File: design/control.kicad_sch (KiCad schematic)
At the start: 20 parts, among them J3 Conn-OScope, J3 SMB, J4 Conn-OScope, J4 SMA, J5 USB_C_Receptacle_USB2.0_14P, U1 STM32F303RETx, U4 CP2102N-Axx-xQFN20

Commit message: _
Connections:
- net HVSense renamed HVVS
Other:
- note added: "Will trip when HV_CS exceeds DAC1_OUT1"
- note removed: "Will trip when HV_CS exceeds 1.2V"
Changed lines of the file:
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@@
 		)
 	)
-	(text "Will trip when HV_CS\nexceeds 1.2V"
+	(text "Will trip when HV_CS\nexceeds DAC1_OUT1"
 		(exclude_from_sim no)
 		(at 248.92 128.27 0)
@@
 		)
 	)
-	(global_label "HVSense"
+	(global_label "HVVS"
 		(shape input)
 		(at 224.79 49.53 0)
@@
 		)
 		(property "Intersheetrefs" "${INTERSHEET_REFS}"
-			(at 235.7581 49.53 0)
+			(at 232.4924 49.53 0)
 			(effects
 				(font

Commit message: _
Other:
- note removed: "For a prototype it might be worth breaking out a few extra GPIO pins..."
- note removed: "I could also set a custom threshold for this with the DAC whichcwould probably improve resolution"
- note removed: "It might make more sense for PulseSense to go to a comparator, since it could also stop the HV generation when the switch is closed"
- note removed: "Same board that came with the devkit I ordered"
- moved on the sheet: J5, R4, R6, R7, U4

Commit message: Working on high voltage switching
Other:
- company: UNH Resilient Architecture Lab -> University of New Hampshire, Resilient Architecture Lab
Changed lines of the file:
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@@
 		(title "BitCrusher: Affordable, Open Source EMFI Platform")
 		(rev "0.1")
-		(company "UNH Resilient Architecture Lab")
+		(company "University of New Hampshire, Resilient Architecture Lab")
 		(comment 1 "Advisor: Dean Sullivan")
 		(comment 2 "Author: George Crane")

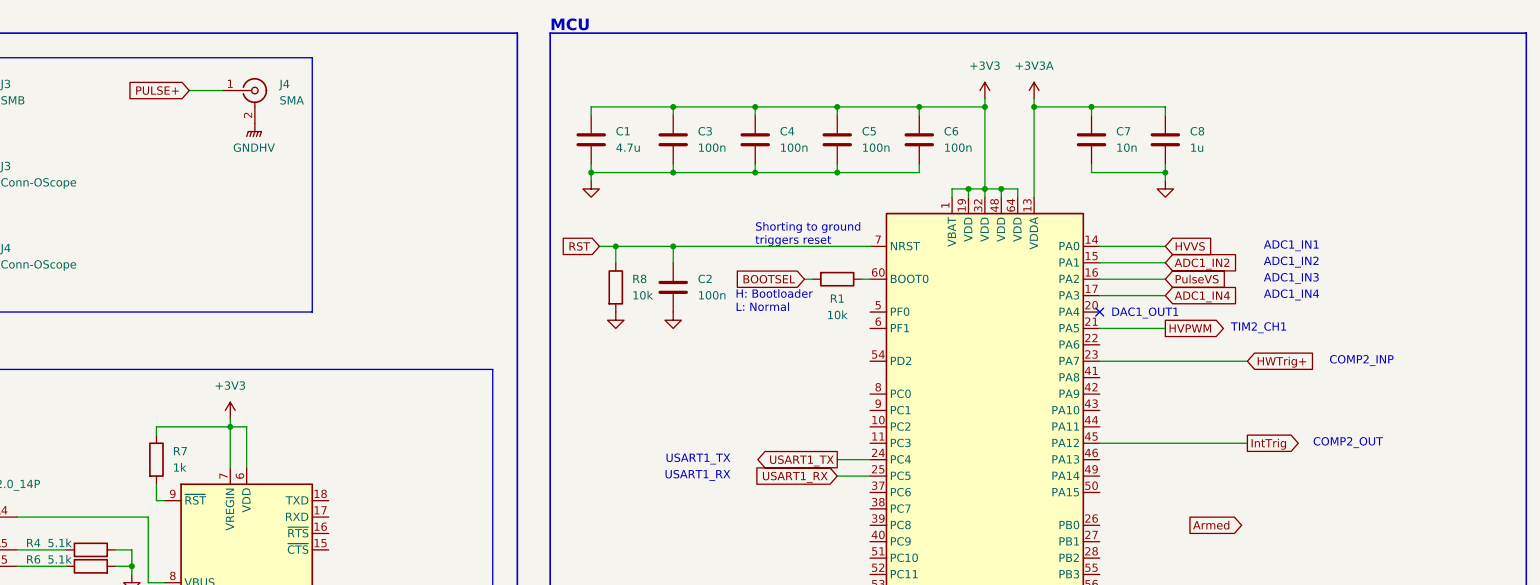
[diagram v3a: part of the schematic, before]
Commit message: assembling final components for HV switching
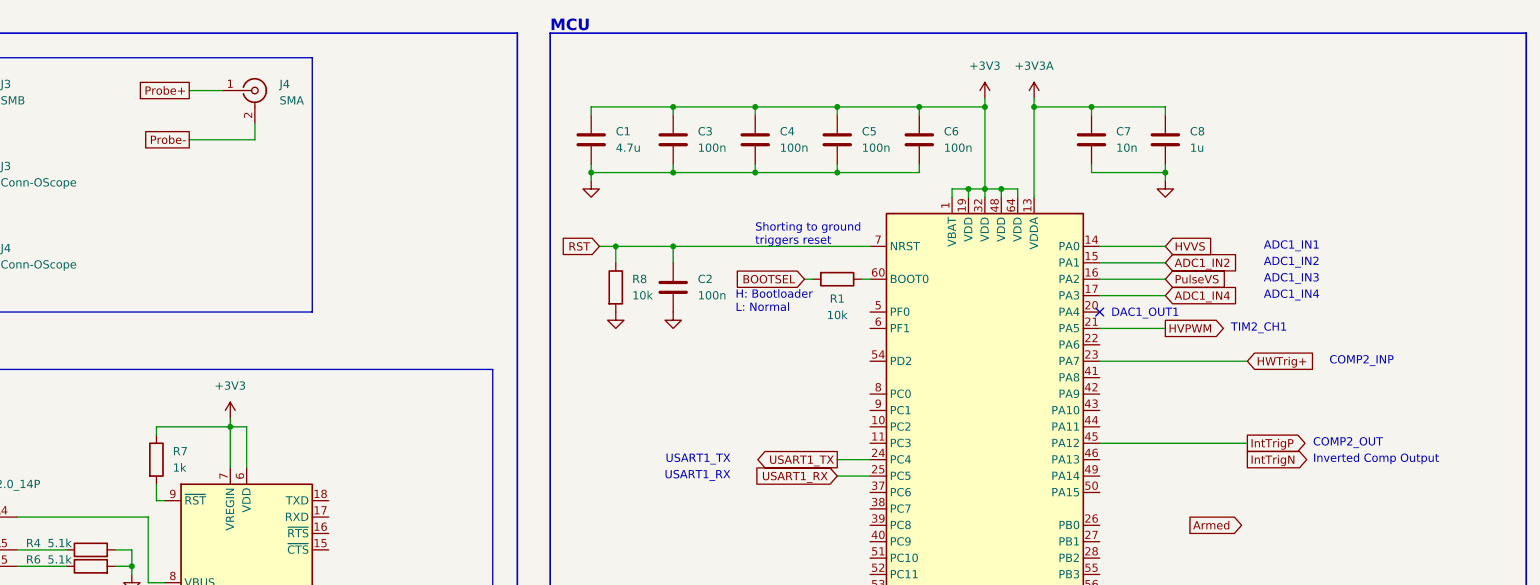
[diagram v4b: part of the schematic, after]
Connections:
- net GNDHV renamed Probe-
- net IntTrig renamed IntTrigP
- net PULSE+ renamed Probe+
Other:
- note added: "Inverted Comp Output"
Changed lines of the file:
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@@
+		)
+	)
+	(text "Inverted Comp Output"
+		(exclude_from_sim no)
+		(at 247.65 82.55 0)
+		(effects
+			(font
+				(size 1.27 1.27)
+			)
+			(justify left)
 		)
 	)
@@
 	(wire
 		(pts
+			(xy 83.82 33.02) (xy 83.82 30.48)
+		)
+		(stroke
+			(width 0)
+			(type default)
+		)
+	)
+	(wire
+		(pts
 			(xy 139.7 49.53) (xy 148.59 49.53)
 		)
@@
 		(pts
 			(xy 30.48 38.1) (xy 35.56 38.1)
+		)
+		(stroke
+			(width 0)
+			(type default)
+		)
+	)
+	(wire
+		(pts
+			(xy 73.66 33.02) (xy 83.82 33.02)
 		)
 		(stroke
@@
 		)
 	)
-	(global_label "IntTrig"
+	(global_label "IntTrigN"
+		(shape output)
+		(at 237.49 82.55 0)
+		(fields_autoplaced yes)
+		(effects
+			(font
+				(size 1.27 1.27)
+			)
+			(justify left)
+		)
+		(property "Intersheetrefs" "${INTERSHEET_REFS}"
+			(at 247.7928 82.55 0)
+			(effects
+				(font
+					(size 1.27 1.27)
+				)
+				(justify left)
+				(hide yes)
+			)
+		)
+	)
+	(global_label "Probe-"
+		(shape passive)
+		(at 73.66 33.02 180)
+		(fields_autoplaced yes)
+		(effects
+			(font
+				(size 1.27 1.27)
+			)
+			(justify right)
+		)
+		(property "Intersheetrefs" "${INTERSHEET_REFS}"
+			(at 64.7709 33.02 0)
+			(effects
+				(font
+					(size 1.27 1.27)
+				)
+				(justify right)
+				(hide yes)
+			)
+		)
+	)
+	(global_label "IntTrigP"
 		(shape output)
 		(at 237.49 80.01 0)
@@
 		)
 		(property "Intersheetrefs" "${INTERSHEET_REFS}"
-			(at 246.4623 80.01 0)
+			(at 247.7323 80.01 0)
 			(effects
 				(font
@@
 		)
 	)
-	(global_label "PULSE+"
-		(shape input)
+	(global_label "Probe+"
+		(shape passive)
 		(at 73.66 25.4 180)
 		(fields_autoplaced yes)
@@
 		)
 		(property "Intersheetrefs" "${INTERSHEET_REFS}"
-			(at 63.1153 25.4 0)
+			(at 64.7709 25.4 0)
 			(effects
 				(font
@@
 					(unit 1)
 				)
-			)
-		)
-	)
-	(symbol
-		(lib_id "power:GNDPWR")
-		(at 83.82 30.48 0)
-		(unit 1)
-		(exclude_from_sim no)
-		(in_bom yes)
-		(on_board yes)
-		(dnp no)
-		(fields_autoplaced yes)
-		(property "Reference" "#PWR018"
-			(at 83.82 35.56 0)
-			(effects
-				(font
-					(size 1.27 1.27)
-				)
-				(hide yes)
-			)
-		)
-		(property "Value" "GNDHV"
-			(at 83.693 34.29 0)
-			(effects
-				(font
-					(size 1.27 1.27)
-				)
-			)
-		)
-		(property "Footprint" ""
-			(at 83.82 31.75 0)
-			(effects
-				(font
-					(size 1.27 1.27)
-				)
-				(hide yes)
-			)
-		)
-		(property "Datasheet" ""
-			(at 83.82 31.75 0)
-			(effects
-				(font
-					(size 1.27 1.27)
-				)
-				(hide yes)
-			)
-		)
-		(property "Description" "Power symbol creates a global label with name \"GNDPWR\" , global ground"
-			(at 83.82 30.48 0)
-			(effects
-				(font
-					(size 1.27 1.27)
-				)
-				(hide yes)
-			)
-		)
-		(pin "1"
-		)
-		(instances
-			(project "BitCrusher"
-				(path "/e1be550d-9ce6-42b1-a89a-c00b9d7586dd/29f45a98-1f25-4a6e-8231-3aa3a650ea17"
-					(reference "#PWR018")
-					(unit 1)
-				)

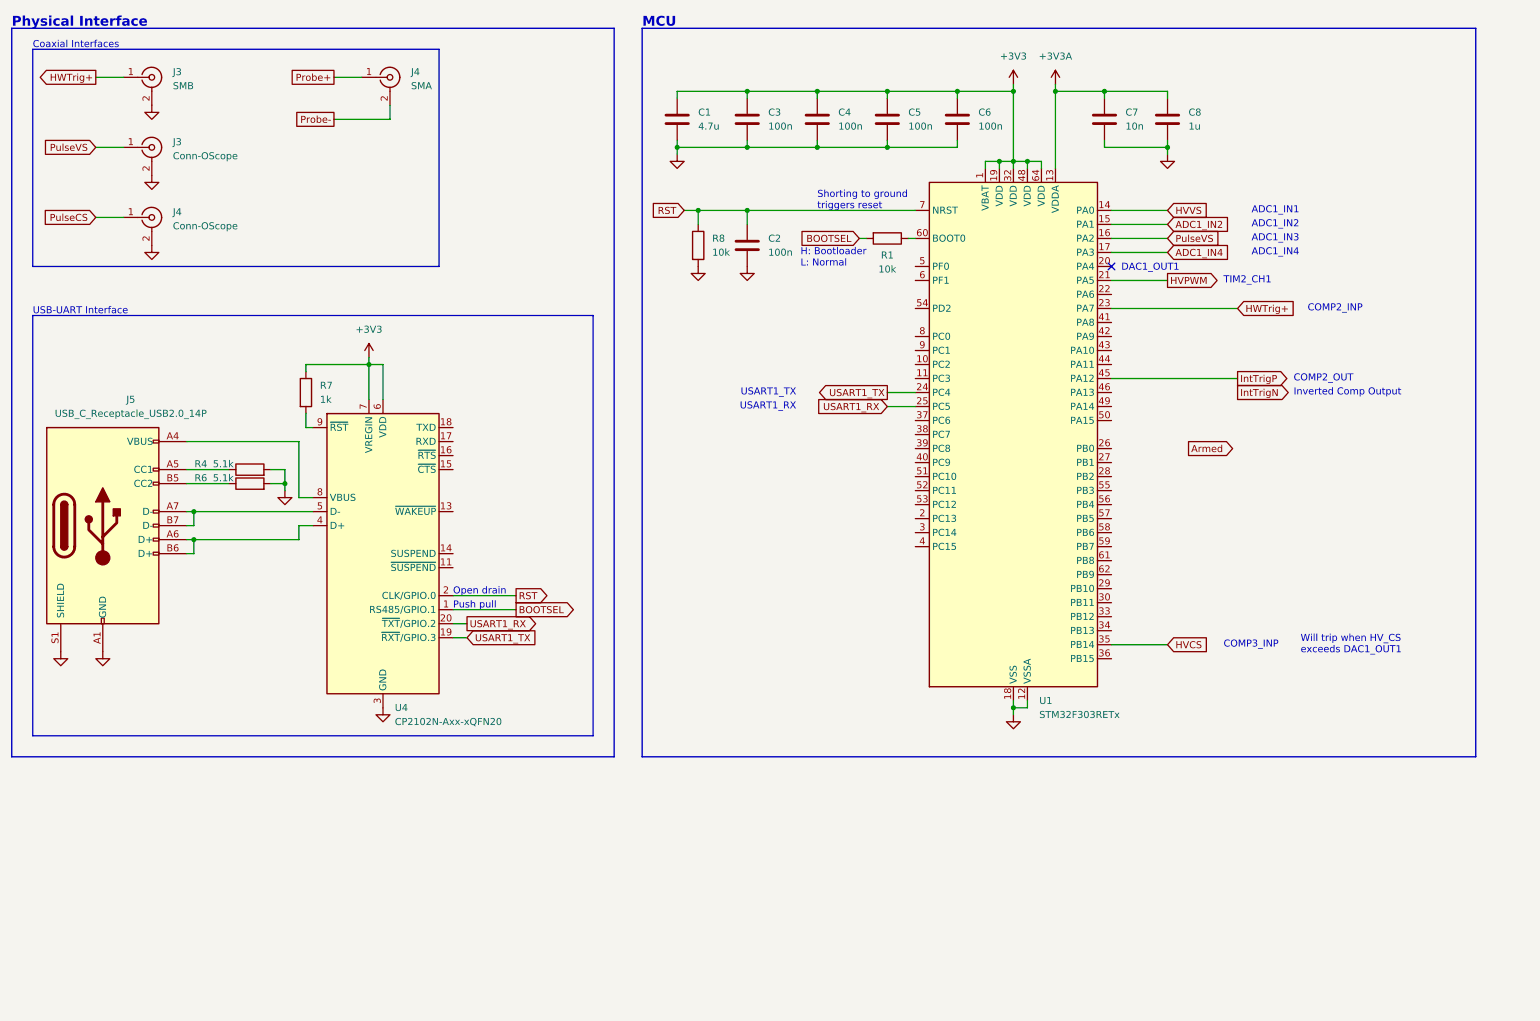
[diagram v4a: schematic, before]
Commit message: Working on probe voltage and current sense circuits
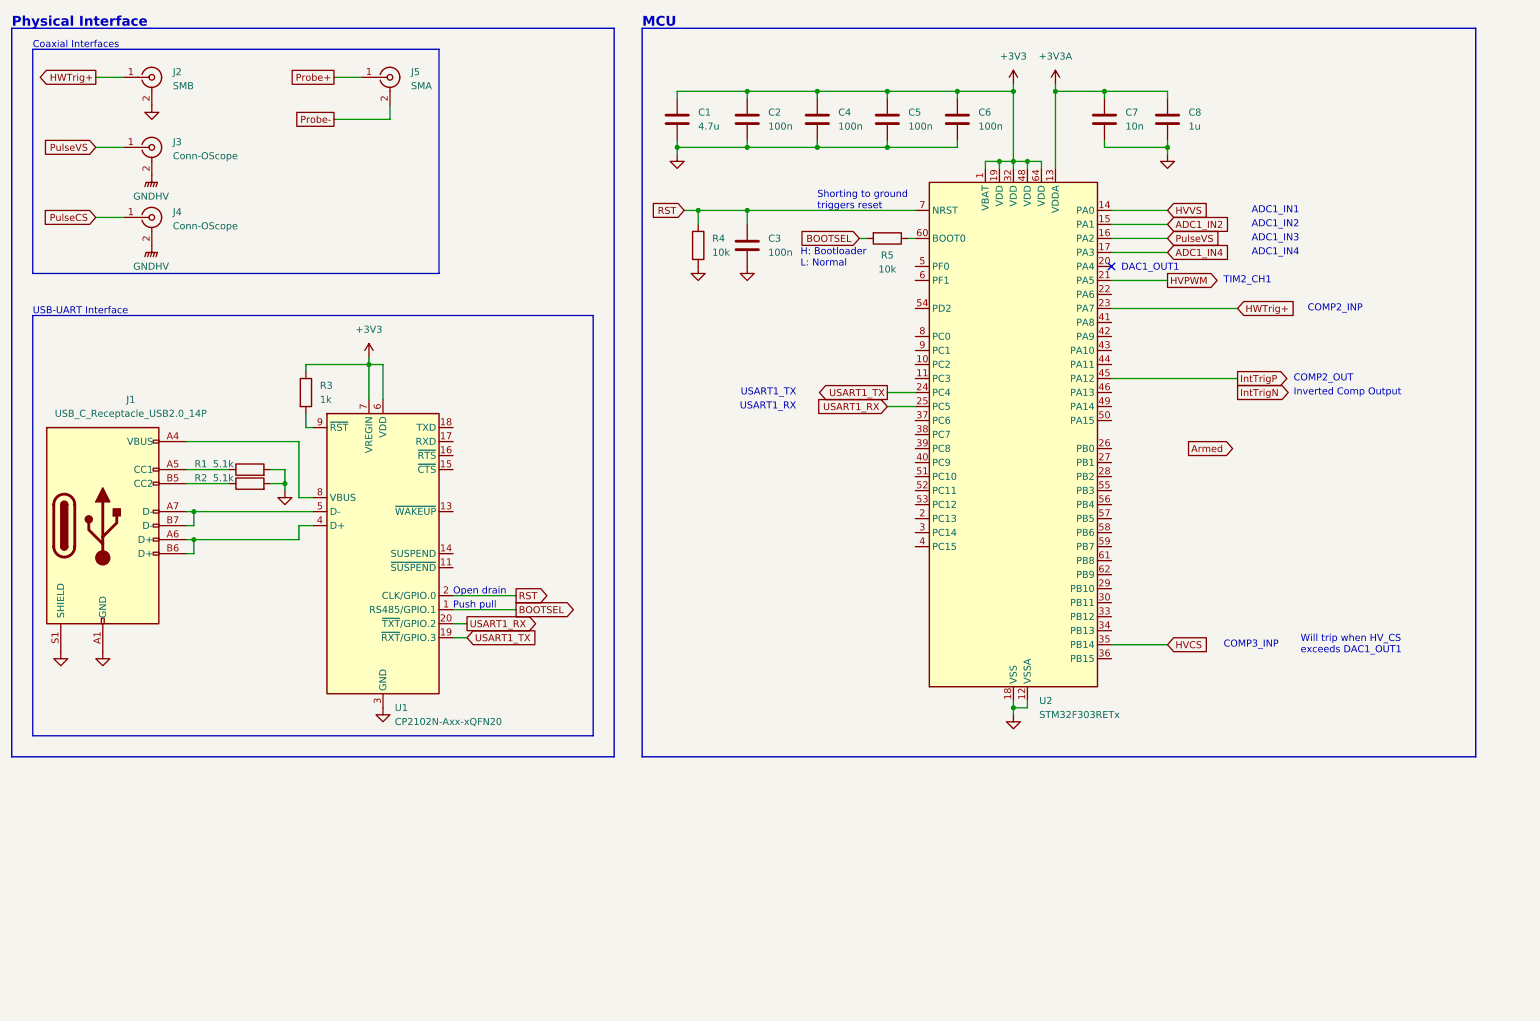
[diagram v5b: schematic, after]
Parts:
- renumbered C3 to C2, C2 to C3, J5 to J1, J3 to J2, J4 to J5, R4 to R1, R6 to R2, R7 to R3, R8 to R4, R1 to R5, U4 to U1, U1 to U2
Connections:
- net GND: no longer J3.2 (Ext), J4.2 (Ext)
- new net GNDHV: J3.2 (Ext), J4.2 (Ext)

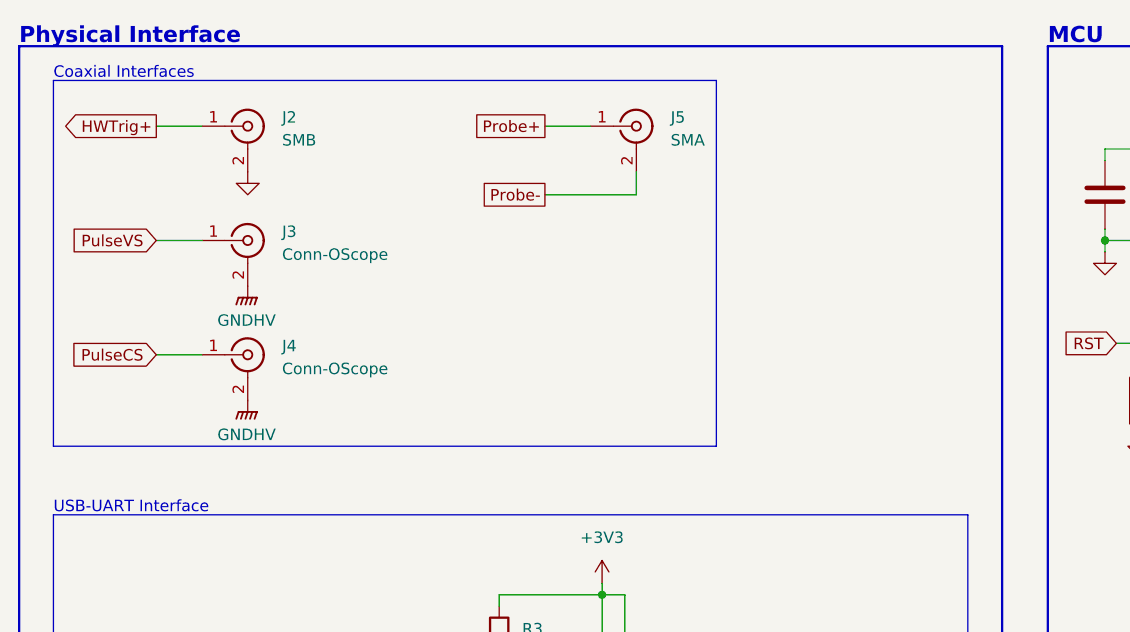
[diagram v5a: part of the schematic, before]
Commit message: Fixed gate drive UVLO
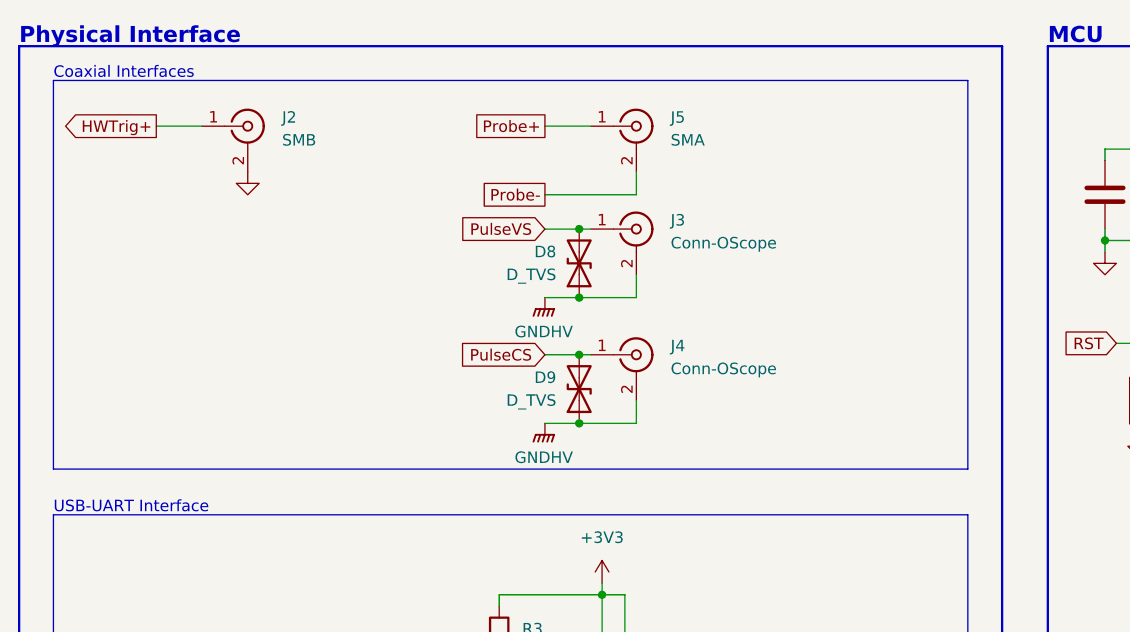
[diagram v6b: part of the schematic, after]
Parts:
- added D8, D9: D_TVS, symbol Device:D_TVS
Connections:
- net GNDHV: now also D8.1 (A1), D9.1 (A1)
- net PulseCS: now also D9.2 (A2)
- net PulseVS: now also D8.2 (A2)
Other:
- moved on the sheet: J3, J4

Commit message: _
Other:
- note removed: "Inverted Comp Output"
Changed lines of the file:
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@@
-		)
-	)
-	(text "Inverted Comp Output"
-		(exclude_from_sim no)
-		(at 247.65 82.55 0)
-		(effects
-			(font
-				(size 1.27 1.27)
-			)
-			(justify left)
 		)
 	)
@@
 		)
 	)
-	(global_label "IntTrigN"
+	(global_label "PulseEN"
 		(shape output)
 		(at 237.49 82.55 0)
@@
 		)
 		(property "Intersheetrefs" "${INTERSHEET_REFS}"
-			(at 247.7928 82.55 0)
+			(at 248.1556 82.55 0)
 			(effects
 				(font
